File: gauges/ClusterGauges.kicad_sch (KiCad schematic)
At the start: 95 parts, among them J1 DTM06-3S nickel, 12V input + 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, J2 SWD Tag-Connect, J7 DTM06-5S nickel, CAN0 + 3x se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, J8 KK-254 22-27-2031, private li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, J9 KK-254 22-27-2021, Hall speed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, Q1 PMV55ENEA ideal diode (DGATE), Q2 PMV37ENEA automotive (AEC-Q10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, Q3 PMV55ENEA pass (HGATE), U1 NXP S32K144 automotive (AEC-Q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, U10 TCAN1044V-Q1 (AEC-Q100 G1), U2 LMR33630-Q1 (AEC-Q100 G1), U3 LM74930-Q1 (AEC-Q100 G1), U4 TLV733P-Q1 (AEC-Q100 G1), U5 NXP TJA1043T automotive CAN t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, U6 Raystar RFA401280B-AYW-DNF1 -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, U7 Raystar RFA401280B-AYW-DNF1 -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, U8 Raystar RFA401280B-AYW-DNF1 -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, U9 Raystar RFA401280B-AYW-DNF1 -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, Y1 8MHz (AEC-Q200)

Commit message: gauges rev C: six 12 V-active indicator-lamp inputs and a tach input
1966 Mustang lamps are 12 V-active (user-confirmed), tach input wanted.
- J10 (7-pin KK 254): left/right turn, high beam, brake, alternator, oil + GND.
  Each input: 33k/15k divider, BAV99-Q clamp, 10 nF filter, DNP 4.7k pull-up
  for a ground-switched lamp (firmware inverts that channel).
- J11 tach: two 18k 1206 (200 V) in series + 15k, 2.2 nF, clamp, DNP pull-up
  for open-collector outputs. Coil-negative use on a points system is not
  validated. MCU pins: tach = pin 57 (FTM1_CH5), lamps = pins 35/36/37/38/43/44.
- Protocol: Indicators (0x303), InputConfig (0x420), RpmFromTach status bit.
- Layout: new zone next to the MCU, battery divider moved next to the ADC.
  Sender ADC nets 242-348 mm -> 72-95 mm; lamp nets 75-97 mm, tach 103 mm.
- Catalog: 1206 200 V resistors and 2.2 nF (both PATTERN, confirm in cart).

ERC unchanged (4 known items), 0 unconnected, DRC accepted categories only.

Co-Authored-By: Claude Sonnet 5.5 <noreply@anthropic.com>
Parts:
- added C50: 10nF input filter, Left turn (AEC-Q200), Capacitor_SMD:C_0603_1608Metric, symbol ClusterGauges:C_V
- added C51: 10nF input filter, Right turn (AEC-Q200), Capacitor_SMD:C_0603_1608Metric, symbol ClusterGauges:C_V
- added C52: 10nF input filter, High beam (AEC-Q200), Capacitor_SMD:C_0603_1608Metric, symbol ClusterGauges:C_V
- added C53: 10nF input filter, Brake / parking brake (AEC-Q20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, Capacitor_SMD:C_0603_1608Metric, symbol ClusterGauges:C_V
- added C54: 10nF input filter, Alternator / charge (AEC-Q200), Capacitor_SMD:C_0603_1608Metric, symbol ClusterGauges:C_V
- added C55: 10nF input filter, Oil pressure (AEC-Q200), Capacitor_SMD:C_0603_1608Metric, symbol ClusterGauges:C_V
- added C56: 2.2nF input filter, tach (AEC-Q200), Capacitor_SMD:C_0603_1608Metric, symbol ClusterGauges:C_V
- added D16: BAV99-Q input clamp, Left turn (AEC-Q101), Package_TO_SOT_SMD:SOT-23, symbol ClusterGauges:D_BAV99
- added D17: BAV99-Q input clamp, Right turn (AEC-Q101), Package_TO_SOT_SMD:SOT-23, symbol ClusterGauges:D_BAV99
- added D18: BAV99-Q input clamp, High beam (AEC-Q101), Package_TO_SOT_SMD:SOT-23, symbol ClusterGauges:D_BAV99
- added D19: BAV99-Q input clamp, Brake / parking brake (AEC-Q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, Package_TO_SOT_SMD:SOT-23, symbol ClusterGauges:D_BAV99
- added D20: BAV99-Q input clamp, Alternator / charge (AEC-Q10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, Package_TO_SOT_SMD:SOT-23, symbol ClusterGauges:D_BAV99
- added D21: BAV99-Q input clamp, Oil pressure (AEC-Q101), Package_TO_SOT_SMD:SOT-23, symbol ClusterGauges:D_BAV99
- added D22: BAV99-Q input clamp, tach (AEC-Q101), Package_TO_SOT_SMD:SOT-23, symbol ClusterGauges:D_BAV99
- added J10: KK-254 22-27-2071, indicator lamp inputs (6 x 12 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, Connector_Molex:Molex_KK-254_AE-6410-07A_1x07_P2.54mm_Vertical, symbol ClusterGauges:CONN_LAMPS
- added J11: KK-254 22-27-2021, tach input (signal + ground), Connector_Molex:Molex_KK-254_AE-6410-02A_1x02_P2.54mm_Vertical, symbol ClusterGauges:CONN_TACH
- added R58: 33k series, Left turn (AEC-Q200), Resistor_SMD:R_0603_1608Metric, symbol ClusterGauges:R_V
- added R59: 15k divider bottom, Left turn (AEC-Q200), Resistor_SMD:R_0603_1608Metric, symbol ClusterGauges:R_V
- added R60: 4.7k pull-up to VIN_PROT, DNP: fit only if the Le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, Resistor_SMD:R_0603_1608Metric, symbol ClusterGauges:R_V
- added R61: 33k series, Right turn (AEC-Q200), Resistor_SMD:R_0603_1608Metric, symbol ClusterGauges:R_V
- added R62: 15k divider bottom, Right turn (AEC-Q200), Resistor_SMD:R_0603_1608Metric, symbol ClusterGauges:R_V
- added R63: 4.7k pull-up to VIN_PROT, DNP: fit only if the Ri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, Resistor_SMD:R_0603_1608Metric, symbol ClusterGauges:R_V
- added R64: 33k series, High beam (AEC-Q200), Resistor_SMD:R_0603_1608Metric, symbol ClusterGauges:R_V
- added R65: 15k divider bottom, High beam (AEC-Q200), Resistor_SMD:R_0603_1608Metric, symbol ClusterGauges:R_V
- added R66: 4.7k pull-up to VIN_PROT, DNP: fit only if the Hi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, Resistor_SMD:R_0603_1608Metric, symbol ClusterGauges:R_V
- added R67: 33k series, Brake / parking brake (AEC-Q200), Resistor_SMD:R_0603_1608Metric, symbol ClusterGauges:R_V
- added R68: 15k divider bottom, Brake / parking brake (AEC-Q2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, Resistor_SMD:R_0603_1608Metric, symbol ClusterGauges:R_V
- added R69: 4.7k pull-up to VIN_PROT, DNP: fit only if the Br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, Resistor_SMD:R_0603_1608Metric, symbol ClusterGauges:R_V
- added R70: 33k series, Alternator / charge (AEC-Q200), Resistor_SMD:R_0603_1608Metric, symbol ClusterGauges:R_V
- added R71: 15k divider bottom, Alternator / charge (AEC-Q200), Resistor_SMD:R_0603_1608Metric, symbol ClusterGauges:R_V
- added R72: 4.7k pull-up to VIN_PROT, DNP: fit only if the Al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, Resistor_SMD:R_0603_1608Metric, symbol ClusterGauges:R_V
- added R73: 33k series, Oil pressure (AEC-Q200), Resistor_SMD:R_0603_1608Metric, symbol ClusterGauges:R_V
- added R74: 15k divider bottom, Oil pressure (AEC-Q200), Resistor_SMD:R_0603_1608Metric, symbol ClusterGauges:R_V
- added R75: 4.7k pull-up to VIN_PROT, DNP: fit only if the Oi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, Resistor_SMD:R_0603_1608Metric, symbol ClusterGauges:R_V
- added R76, R77: 18k series, tach, 200V (AEC-Q200), Resistor_SMD:R_1206_3216Metric, symbol ClusterGauges:R_1206
- added R78: 15k divider bottom, tach (AEC-Q200), Resistor_SMD:R_0603_1608Metric, symbol ClusterGauges:R_V
- added R79: 4.7k pull-up to VIN_PROT, DNP: fit only for an op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, Resistor_SMD:R_0603_1608Metric, symbol ClusterGauges:R_V
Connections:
- net +3V3: now also D16.2 (K2), D17.2 (K2), D18.2 (K2), D19.2 (K2), D20.2 (K2), D21.2 (K2), D22.2 (K2)
- net GND: now also C50.2, C51.2, C52.2, C53.2, C54.2, C55.2, C56.2, D16.1 (A1), D17.1 (A1), D18.1 (A1), D19.1 (A1), D20.1 (A1), D21.1 (A1), D22.1 (A1), J10.7 (GND), J11.2 (GND), R59.2, R62.2, R65.2, R68.2, R71.2, R74.2, R78.2
- net VIN_PROT: now also R60.1, R63.1, R66.1, R69.1, R72.1, R75.1, R79.1
- new net LAMP_ALT: C54.1, D20.3 (CA), R70.2, R71.1, U1.43 (LAMP_ALT)
- new net LAMP_ALT_RAW: J10.5 (LAMP_ALT), R70.1, R72.2
- new net LAMP_BRAKE: C53.1, D19.3 (CA), R67.2, R68.1, U1.38 (LAMP_BRAKE)
- new net LAMP_BRAKE_RAW: J10.4 (LAMP_BRAKE), R67.1, R69.2
- new net LAMP_HIGH_BEAM: C52.1, D18.3 (CA), R64.2, R65.1, U1.37 (LAMP_HIGH_BEAM)
- new net LAMP_HIGH_BEAM_RAW: J10.3 (LAMP_HIGH_BEAM), R64.1, R66.2
- new net LAMP_OIL: C55.1, D21.3 (CA), R73.2, R74.1, U1.44 (LAMP_OIL)
- new net LAMP_OIL_RAW: J10.6 (LAMP_OIL), R73.1, R75.2
- new net LAMP_TURN_L: C50.1, D16.3 (CA), R58.2, R59.1, U1.35 (LAMP_TURN_L)
- new net LAMP_TURN_L_RAW: J10.1 (LAMP_TURN_L), R58.1, R60.2
- new net LAMP_TURN_R: C51.1, D17.3 (CA), R61.2, R62.1, U1.36 (LAMP_TURN_R)
- new net LAMP_TURN_R_RAW: J10.2 (LAMP_TURN_R), R61.1, R63.2
- new net TACH_IN: C56.1, D22.3 (CA), R77.2, R78.1, U1.57 (TACH_IN)
- new net TACH_MID: R76.2, R77.1
- new net TACH_RAW: J11.1 (TACH_SIG), R76.1, R79.2
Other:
- note added: "REV C: INDICATOR LAMPS (6 x 12 V-ACTIVE) AND TACH INPUT"

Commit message: gauges: dash dimmer input on J10 pin 8 (ADC0_SE7, pin 31)
The 1966 Mustang headlight switch dims the instrument lamps with a rheostat,
so the feed wire is 0 V with lights off and about 4-12 V when on. 22k/6.8k
divider, BAV99-Q clamp, 100 nF filter. J10 becomes 8-circuit (22-27-2081).
Protocol: Indicators gains DashLightsOn and DashDimmerPct. ERC unchanged (4),
0 unconnected, DRC accepted categories only, ADC nets 80-98 mm.

Co-Authored-By: Claude Sonnet 5.5 <noreply@anthropic.com>
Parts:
- added C57: 100nF input filter, dash dimmer (AEC-Q200), Capacitor_SMD:C_0603_1608Metric, symbol ClusterGauges:C_V
- added D23: BAV99-Q input clamp, dash dimmer (AEC-Q101), Package_TO_SOT_SMD:SOT-23, symbol ClusterGauges:D_BAV99
- added R80: 22k divider top, dash dimmer (AEC-Q200), Resistor_SMD:R_0603_1608Metric, symbol ClusterGauges:R_V
- added R81: 6.8k divider bottom, dash dimmer (AEC-Q200), Resistor_SMD:R_0603_1608Metric, symbol ClusterGauges:R_V
- J10: value KK-254 22-27-2071, indicator lamp inputs (6 x 12 V-active + ground) -> KK-254 22-27-2081, indicator lamp inputs (6 x 12 V-active + ground) and dash-dimmer feed; footprint Connector_Molex:Molex_KK-254_AE-6410-07A_1x07_P2.54mm_Vertical -> Connector_Molex:Molex_KK-254_AE-6410-08A_1x08_P2.54mm_Vertical
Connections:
- net +3V3: now also D23.2 (K2)
- net GND: now also C57.2, D23.1 (A1), R81.2
- new net DIM_ADC: C57.1, D23.3 (CA), R80.2, R81.1, U1.31 (DIM_ADC)
- new net DIM_RAW: J10.8 (DIM_RAW), R80.1

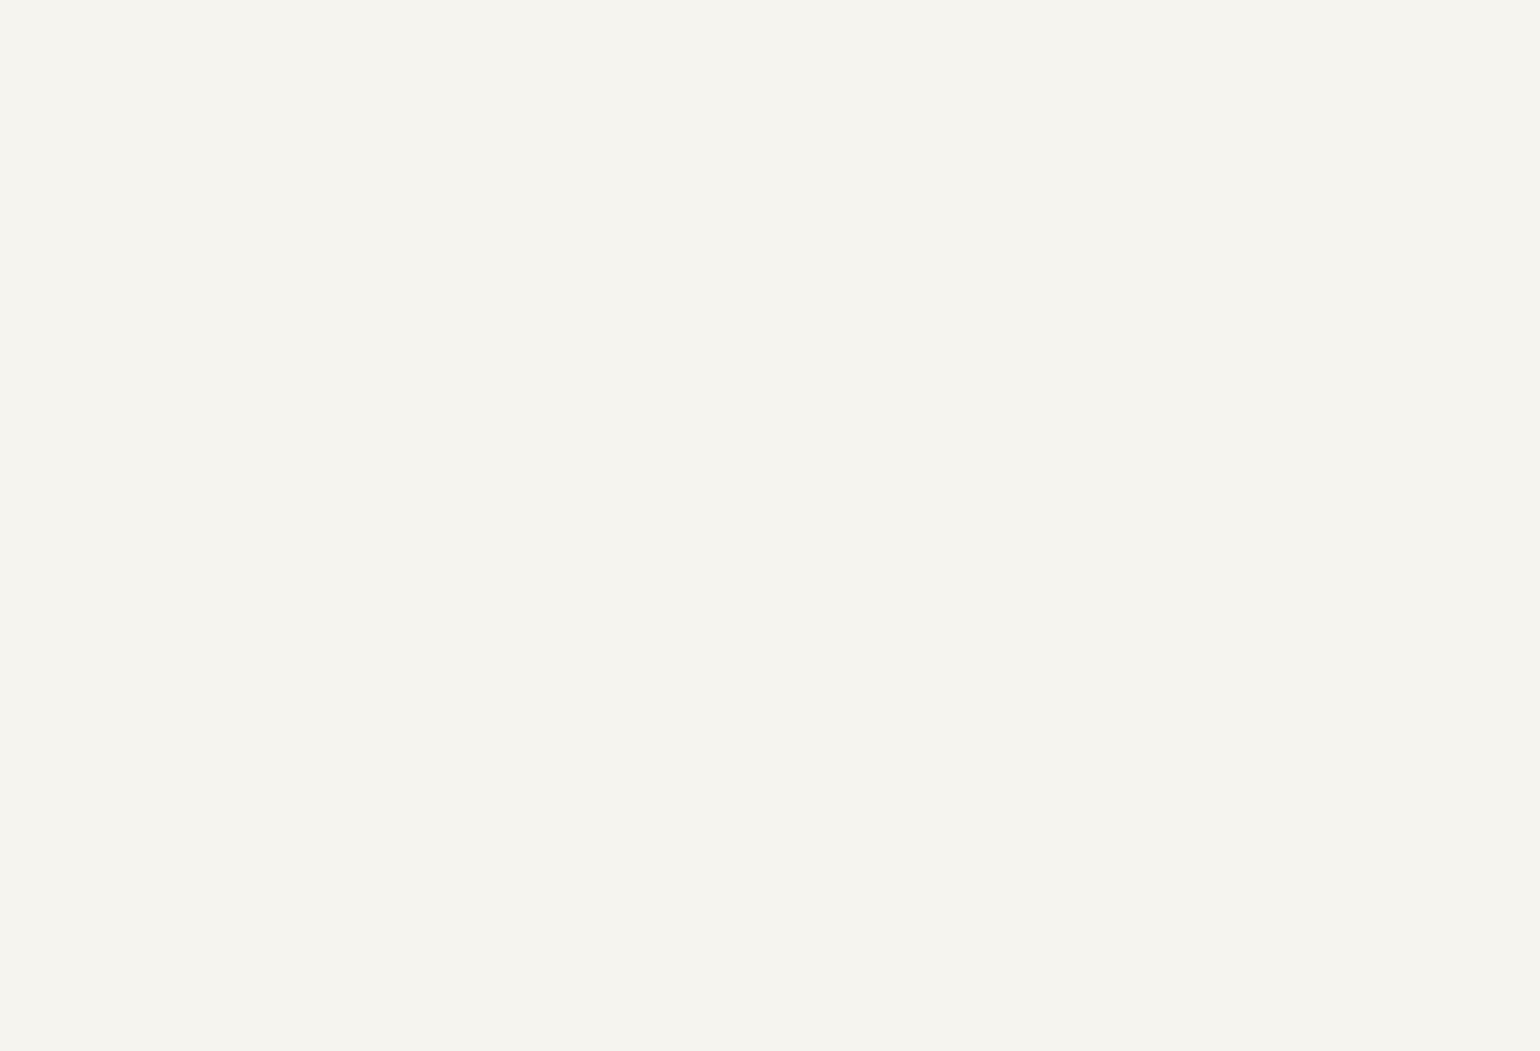
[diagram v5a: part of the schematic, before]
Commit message: Add the physical turn-signal arrows to gauges/: two green LEDs lit straight from the flasher wires
ROHM CSL0902ET1C (AEC-Q102, land pattern from its data sheet) behind the faceplate, each from its LAMP_TURN_x_RAW wire through a 1.8k 1206 resistor, with a BAV99-Q reverse clamp, so they flash like the old bulbs and work with the software off. The J10 sense inputs are unchanged. X positions are placeholders from the concept drawing (TURN_LED_X in build_pcb.py) until the faceplate drawing exists. Re-routed to 0 unconnected nets (real kicad-cli DRC: same four accepted categories as before), BOM updated.

Co-Authored-By: Claude Sonnet 5.5 <noreply@anthropic.com>
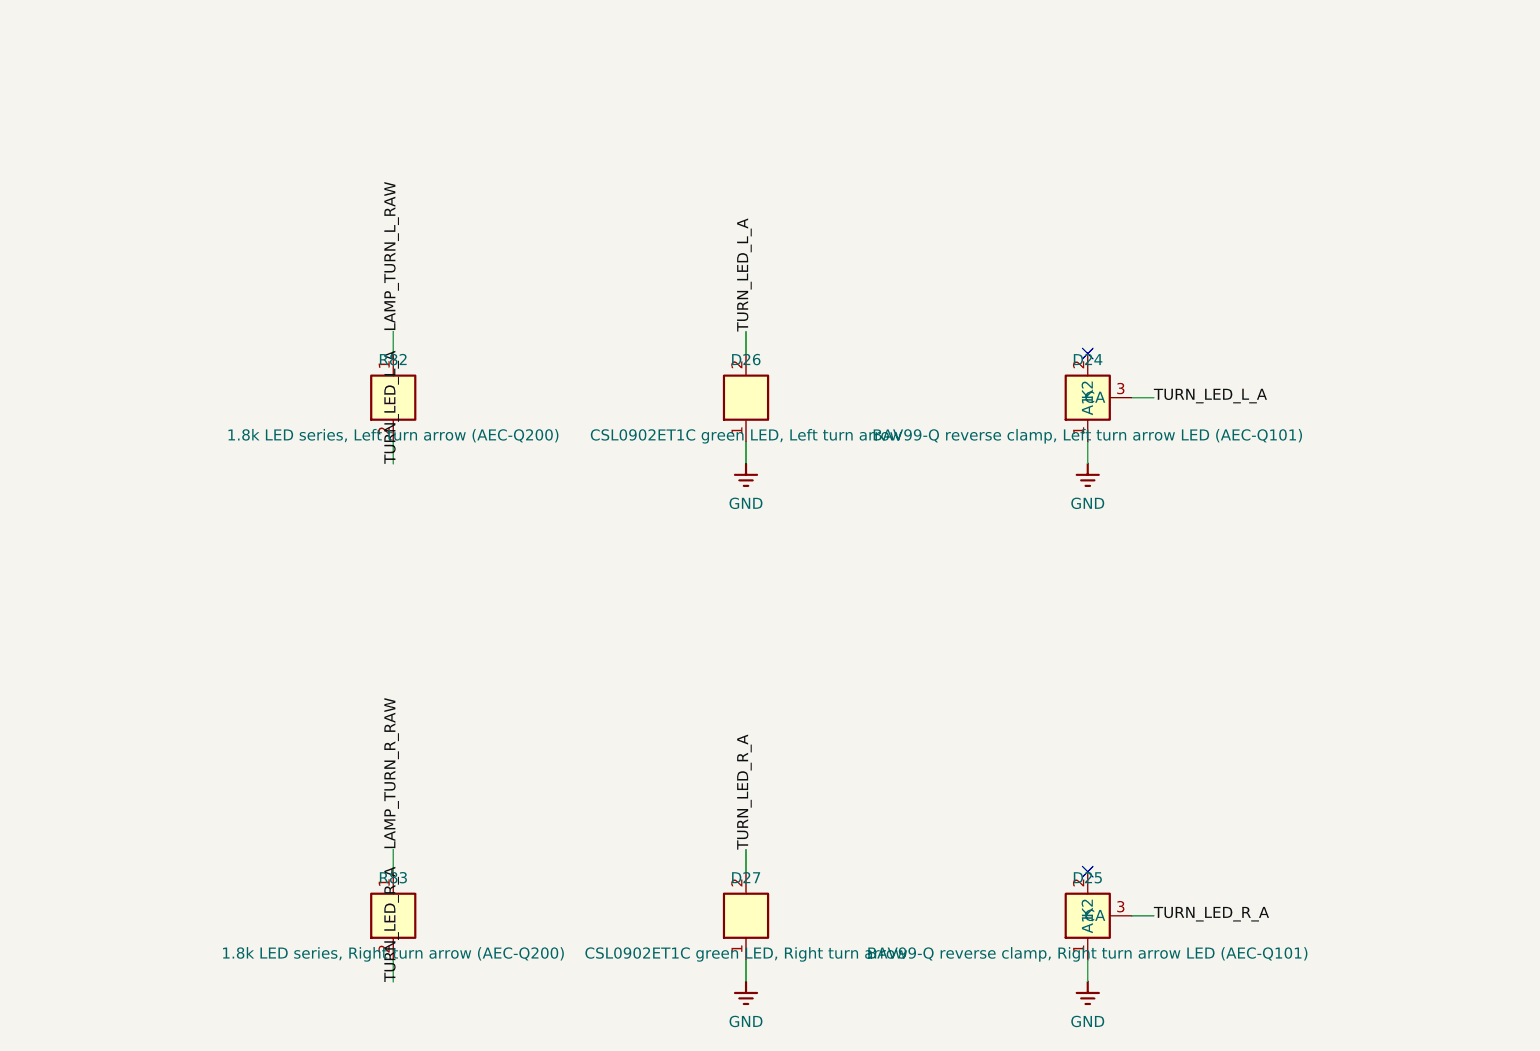
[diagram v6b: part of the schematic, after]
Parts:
- added D24: BAV99-Q reverse clamp, Left turn arrow LED (AEC-Q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, Package_TO_SOT_SMD:SOT-23, symbol ClusterGauges:D_BAV99
- added D25: BAV99-Q reverse clamp, Right turn arrow LED (AEC-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, Package_TO_SOT_SMD:SOT-23, symbol ClusterGauges:D_BAV99
- added D26: CSL0902ET1C green LED, Left turn arrow, ROHM_CSL0902:CSL0902_1608, symbol ClusterGauges:LED_G
- added D27: CSL0902ET1C green LED, Right turn arrow, ROHM_CSL0902:CSL0902_1608, symbol ClusterGauges:LED_G
- added R82: 1.8k LED series, Left turn arrow (AEC-Q200), Resistor_SMD:R_1206_3216Metric, symbol ClusterGauges:R_1206
- added R83: 1.8k LED series, Right turn arrow (AEC-Q200), Resistor_SMD:R_1206_3216Metric, symbol ClusterGauges:R_1206
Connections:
- net GND: now also D24.1 (A1), D25.1 (A1), D26.1 (K), D27.1 (K)
- net LAMP_TURN_L_RAW: now also R82.1
- net LAMP_TURN_R_RAW: now also R83.1
- new net TURN_LED_L_A: D24.3 (CA), D26.2 (A), R82.2
- new net TURN_LED_R_A: D25.3 (CA), D27.2 (A), R83.2
- no-connect marks 40 -> 42

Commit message: Electrical design review: fix gauges J2 pinout and shorted crystal, MCU/CAN decoupling cells, connector TVS, extra input bulk; add review/ scripts and docs/electrical-review.md
Review scripts (review/): netlist vs datasheet pin tables, connector audit, ISO 7637 surge simulation, thermal/derating, DSI impedance, layout checks. gauges/ regenerated and routed: 0 unconnected nets, real DRC in the same four accepted categories. display/ reviewed read-only; its findings are open items in the report.

Co-Authored-By: Claude Sonnet 5.5 <noreply@anthropic.com>
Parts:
- removed R16: 1k fuel pull-up to +3V3 (11mW at a 10R sender) (A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, Resistor_SMD:R_0603_1608Metric, symbol ClusterGauges:R_V
- removed R17: 1k oil pull-up to +3V3 (AEC-Q200), Resistor_SMD:R_0603_1608Metric, symbol ClusterGauges:R_V
- removed R18: 1k coolant temp pull-up to +3V3 (AEC-Q200), Resistor_SMD:R_0603_1608Metric, symbol ClusterGauges:R_V
- added C58: 1uF X7R LDO input (AEC-Q200), Capacitor_SMD:C_0603_1608Metric, symbol ClusterGauges:C_V
- added C59, C60: 10uF 50V X7S extra bulk at VIN_PROT (AEC-Q200), Capacitor_SMD:C_1210_3225Metric, symbol ClusterGauges:C_1210
- added D28: SM24CANB-02HTG TVS on the car CAN bus, at J7 (AEC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, Package_TO_SOT_SMD:SOT-23, symbol ClusterGauges:TVS_ARRAY
- added D29: SM24CANB-02HTG TVS on the fuel and oil sender wir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, Package_TO_SOT_SMD:SOT-23, symbol ClusterGauges:TVS_ARRAY
- added D30: SM24CANB-02HTG TVS on the coolant sender wire, at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, Package_TO_SOT_SMD:SOT-23, symbol ClusterGauges:TVS_ARRAY
- added D31: SM24CANB-02HTG TVS on the private CAN link, at J8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, Package_TO_SOT_SMD:SOT-23, symbol ClusterGauges:TVS_ARRAY
- added D32: SM24CANB-02HTG TVS on the Hall speed wire, at J9 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, Package_TO_SOT_SMD:SOT-23, symbol ClusterGauges:TVS_ARRAY
- added R16: 1k fuel pull-up to +3V3, 1206: a wire shorted to 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, Resistor_SMD:R_1206_3216Metric, symbol ClusterGauges:R_1206
- added R17: 1k oil pull-up to +3V3, 1206 (AEC-Q200), Resistor_SMD:R_1206_3216Metric, symbol ClusterGauges:R_1206
- added R18: 1k coolant temp pull-up to +3V3, 1206 (AEC-Q200), Resistor_SMD:R_1206_3216Metric, symbol ClusterGauges:R_1206
- added R84: 33R SPI SCK series termination at the MCU (AEC-Q2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, Resistor_SMD:R_0603_1608Metric, symbol ClusterGauges:R_V
- added R85: 33R SPI MOSI series termination at the MCU (AEC-Q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, Resistor_SMD:R_0603_1608Metric, symbol ClusterGauges:R_V
- added R86: 100k BL_GATE pull-down, backlights stay off until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, Resistor_SMD:R_0603_1608Metric, symbol ClusterGauges:R_V
- added R87: 100k CAN0_EN pull-down, defined state while the M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, Resistor_SMD:R_0603_1608Metric, symbol ClusterGauges:R_V
- added R88: 100k CAN0_STB_N pull-down, defined state while th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, Resistor_SMD:R_0603_1608Metric, symbol ClusterGauges:R_V
- J2: value SWD Tag-Connect -> SWD Tag-Connect TC2030-IDC-NL (pin order per Tag-Connect: 1 VCC, 2 SWDIO, 3 nRESET, 4 SWCLK, 5 GND, 6 SWO)
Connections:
- net +3V3: now also J2.1 (VCC), R16.1, R17.1, R18.1; no longer J2.2 (VCC)
- net +5V: now also C58.1
- net BL_GATE: now also R86.1
- net CAN0_EN: now also R87.1
- net CAN0_H: now also D28.1 (IO1)
- net CAN0_L: now also D28.2 (IO2)
- net CAN0_STB_N: now also R88.1
- net CAN1_H: now also D31.1 (IO1)
- net CAN1_L: now also D31.2 (IO2)
- net GND: now also J2.5 (GND), Y1.2 (GND), Y1.4 (GND), C58.2, C59.2, C60.2, D28.3 (COM), D29.3 (COM), D30.3 (COM), D31.3 (COM), D32.3 (COM), R86.2, R87.2, R88.2; no longer J2.6 (GND)
- net LPSPI2_SCK: now also R84.2; no longer U1.29 (LPSPI2_SCK)
- net LPSPI2_SOUT: now also R85.2; no longer U1.25 (LPSPI2_SOUT)
- net OSC_IN: no longer Y1.3 (OSC_IN)
- net OSC_OUT: now also Y1.3 (XTAL2); no longer Y1.2 (OSC_OUT), Y1.4 (OSC_OUT)
- net RESET: now also J2.3 (nRESET); no longer J2.5 (RST)
- net SENDER_FUEL: now also D29.1 (IO1), R16.2
- net SENDER_OIL: now also D29.2 (IO2), R17.2
- net SENDER_TEMP: now also D30.1 (IO1), R18.2
- net SPEED_RAW: now also D32.1 (IO1)
- net SWCLK: now also J2.4 (SWCLK); no longer J2.3 (SWCLK)
- net SWDIO: now also J2.2 (SWDIO); no longer J2.1 (SWDIO)
- net VIN_PROT: now also C59.1, C60.1
- new net LPSPI2_SCK_MCU: R84.1, U1.29 (LPSPI2_SCK)
- new net LPSPI2_SOUT_MCU: R85.1, U1.25 (LPSPI2_SOUT)
- no-connect marks 42 -> 44
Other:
- note added: "REVIEW 2026-10-17: CONNECTOR PROTECTION, SPI SERIES TERMINATION, EXTRA BULK, BACKLIGHT GATE PULL-DOWN"
